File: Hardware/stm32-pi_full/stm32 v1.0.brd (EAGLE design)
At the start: 131.4 x 105.8 mm, 292 parts, among them J1 SOLDERJUMPERNO, J2 5-1814400-1, U1 ESP32-WROOM-32D, Y1 6MM_3.5MM_CRYSTAL

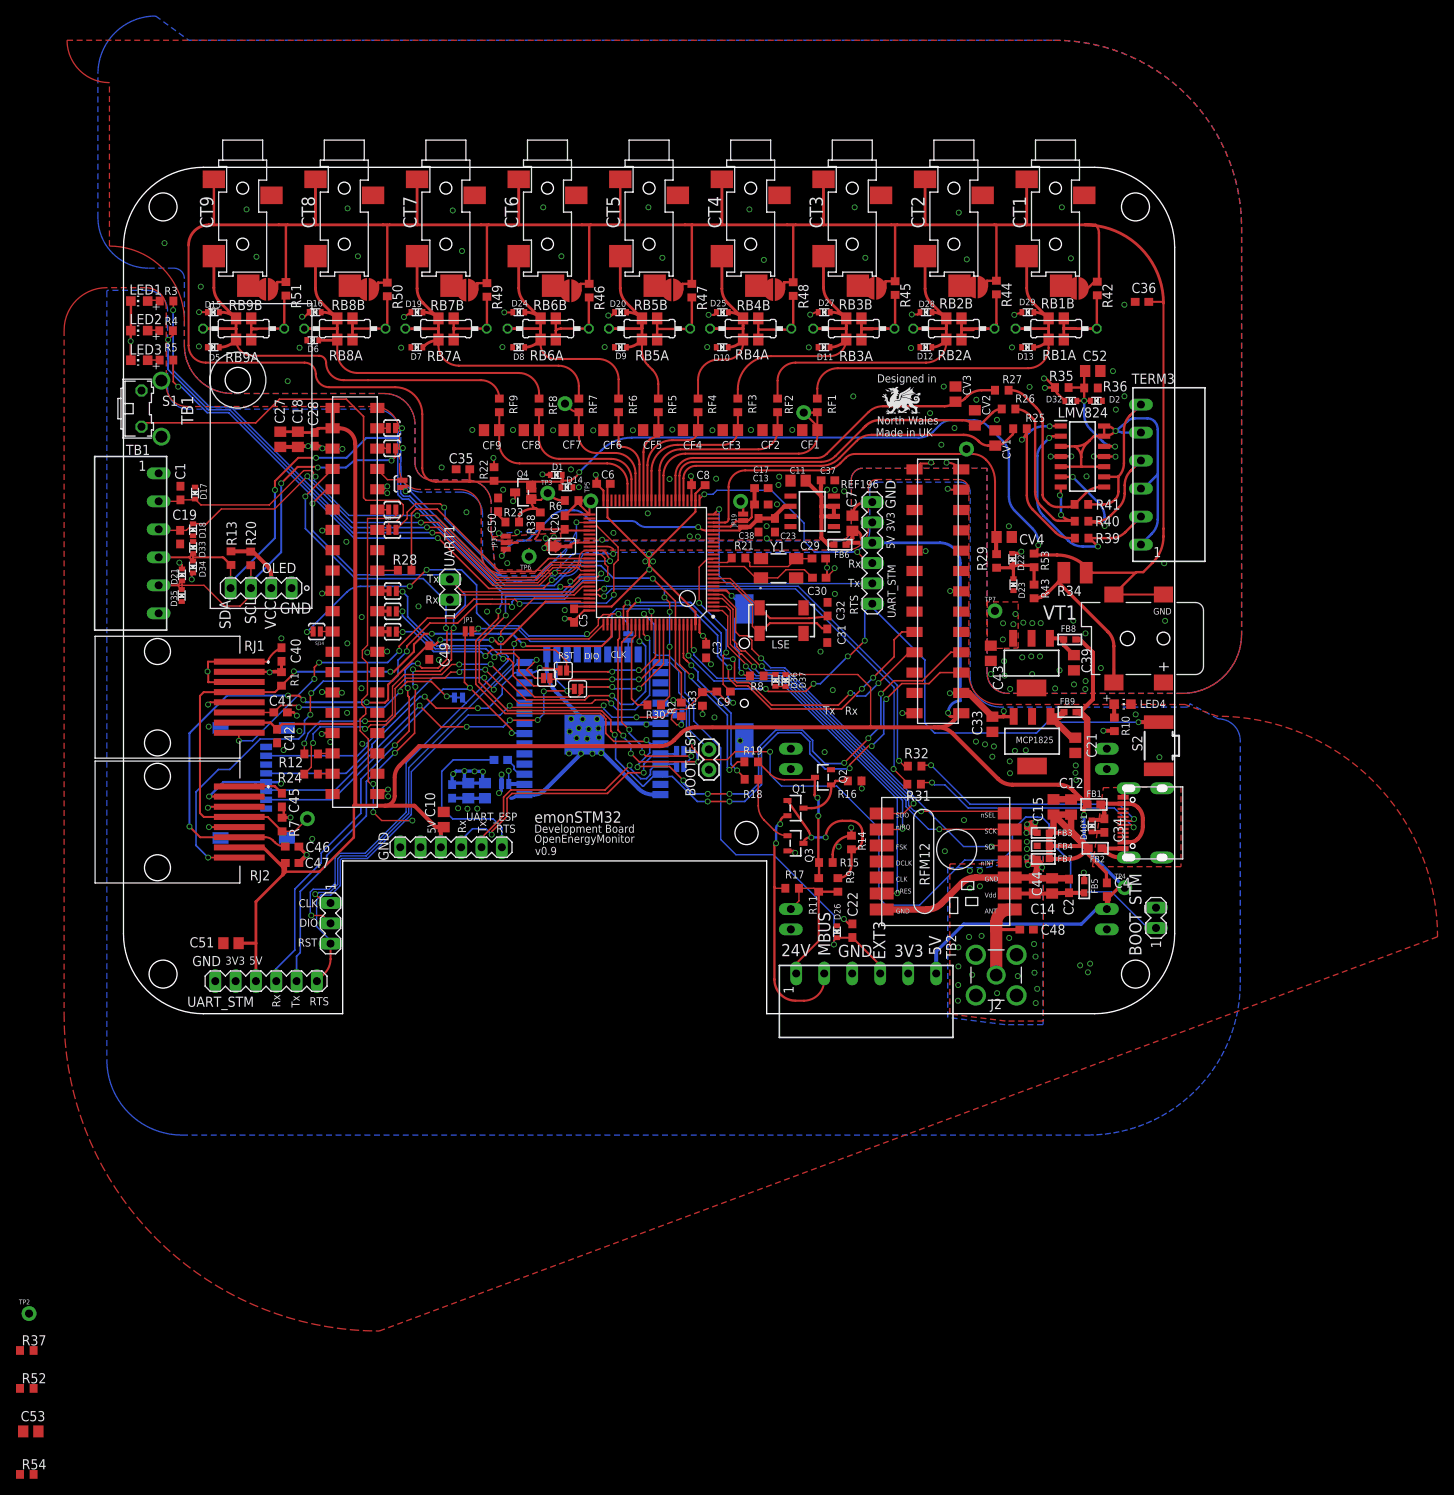
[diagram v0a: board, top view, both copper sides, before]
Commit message: UART Tx improvments and v1.0 HW change
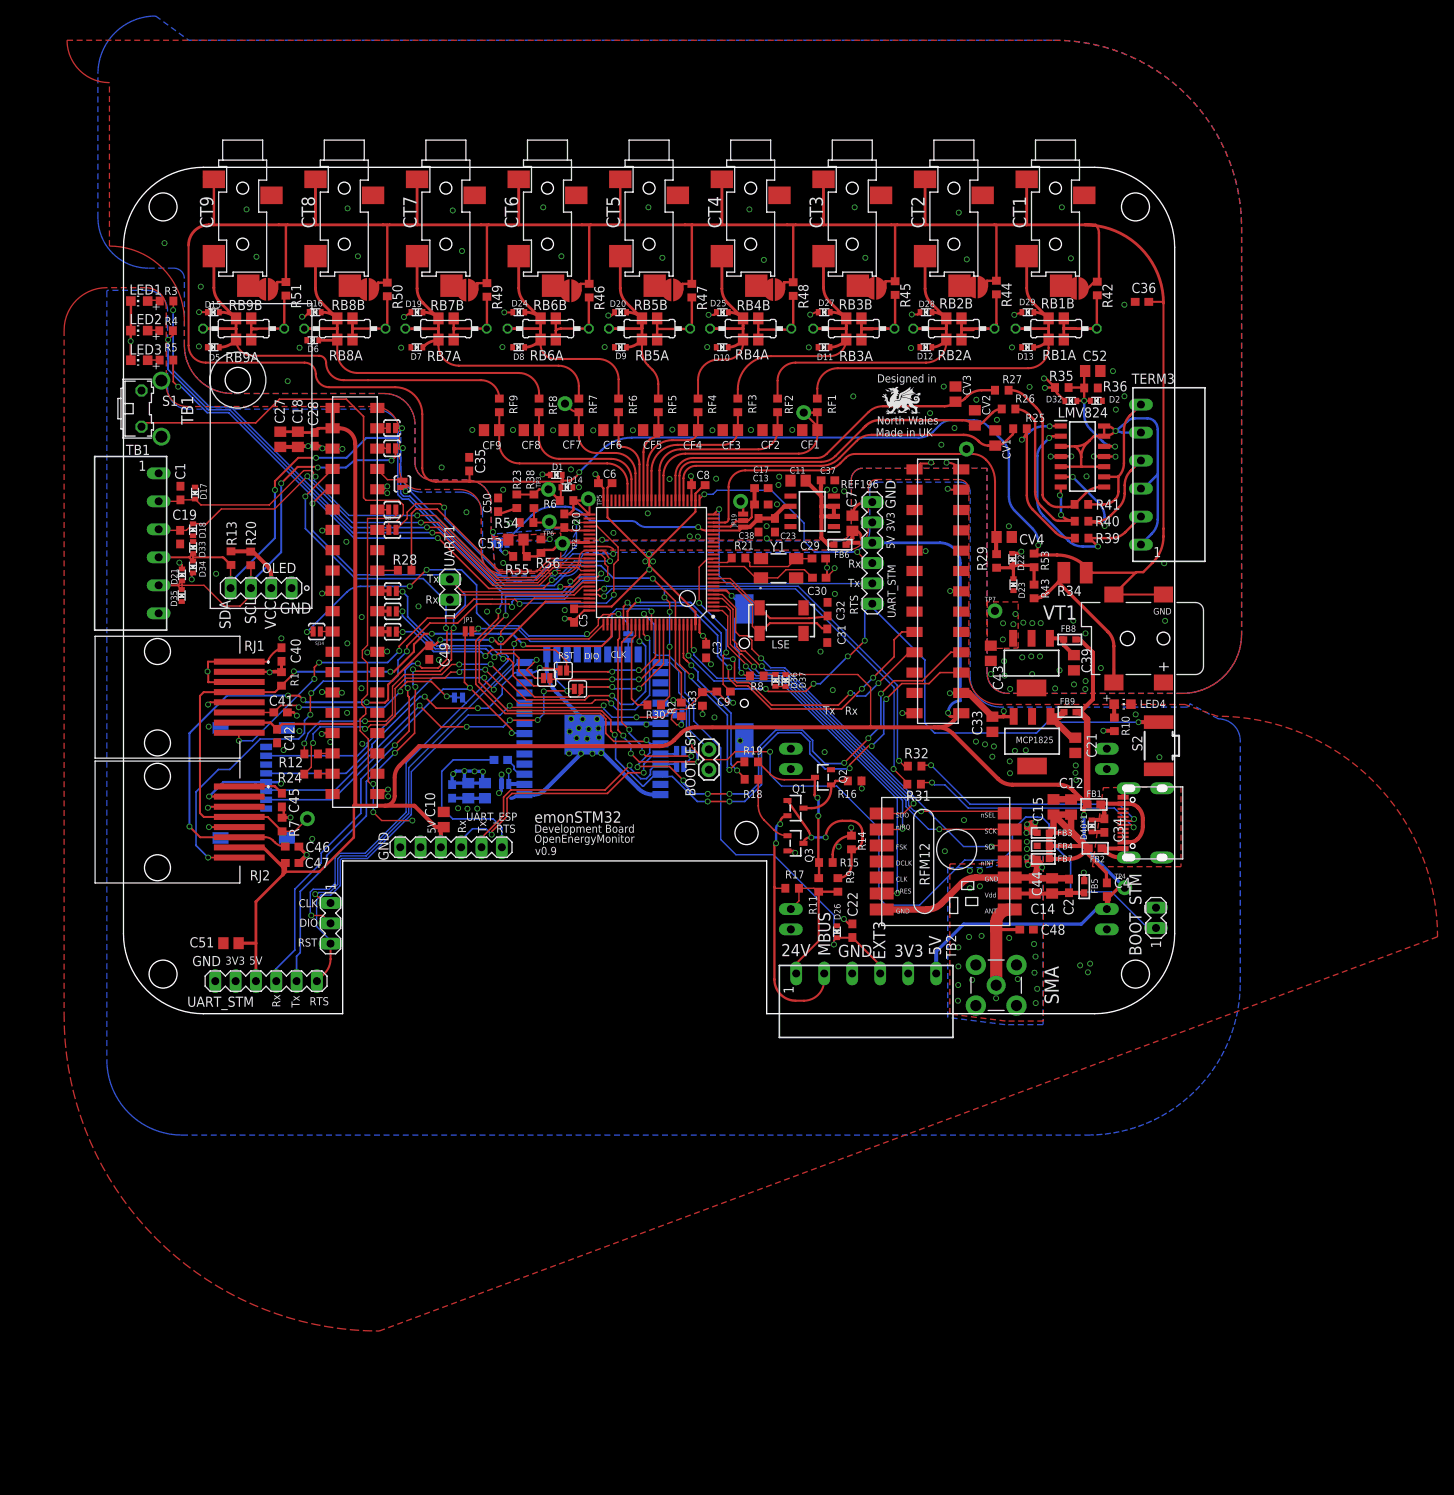
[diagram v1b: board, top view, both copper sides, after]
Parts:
- removed J2: 5-1814400-1, 5-1814400-1 sma connector:518144001
- removed JP2: JUMPER-SMT_2_NO_NO-SILK, SparkFun-Jumpers:SMT-JUMPER_2_NO_NO-SILK
- removed Q4: (no value), microbuilder:SOT23-WIDE
- removed R22, R37, R52: 10k, resistor:R0603
- removed SJ1: (no value), jumper-con_db:SJ-CON
- added R55: 9k, resistor:R0603
- added R56: 1k, resistor:R0603
- added SMA: 5-1814400-1, 5-1814400-1 sma connector:518144001
- R38: value 10k -> 4k
- R54: value 10k -> 1k
- moved R54 134.4 mm to (50.4, 61.4), turned to 180 degrees
- moved C53 126.9 mm to (49.1, 59.3), turned to 180 degrees
- moved TP2 117.1 mm to (54.9, 58.8)
- moved TP6 5.02 mm to (53.2, 61.5)
- moved R23 2.66 mm to (49.2, 64.1), turned to 90 degrees
- moved R38 2.38 mm to (51.3, 64.1)
- moved C35 1.01 mm to (43.2, 68.7), turned to 90 degrees
- moved JP3 0.66 mm to (47.1, 58.9), flipped to the bottom, turned to 0 degrees
- moved R6 0.64 mm to (55.4, 64.1)
- moved TP3 0.48 mm to (53.1, 65.5)
- moved TP5 0.40 mm to (58.1, 64.3)
- moved C6 0.24 mm to (60.2, 66.3)
- moved C20 0.23 mm to (55.1, 61.6)
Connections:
- removed net OPAMP_FB2: JP2.1, Q4.1, R23.2, R38.1, R6.2, TP3.1
- removed net OPAMP_NON-INV+: C53.1, R37.1, R52.2, TP2.1
- net +3V3ANA: no longer Q4.3
- net AGND: now also R56.1; no longer R22.1, R52.1, SJ1.2
- net ANT: now also SMA.1; no longer J2.1
- net BIAS: now also R23.2, R38.1, R6.2, TP3.1; no longer JP2.2, Q4.2, R22.2
- net N$12: now also R55.2; no longer R37.2
- net OPAMP_NON-INVERT+: now also C53.1, R55.1, R56.2, TP2.1; no longer SJ1.1
- net RGND: now also SMA.2, SMA.3, SMA.4, SMA.5; no longer J2.2, J2.3, J2.4, J2.5
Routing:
- net OPAMP_FB2: track 10.3 -> 0.00 mm
- net OPAMP_NON-INVERT+: track 2.74 -> 12.3 mm
- net BIAS: track 486.8 -> 493.3 mm
- net AGND: track 22.8 -> 18.2 mm, vias 106 -> 103
- net VREF+: track 41.2 -> 39.5 mm, vias 2 -> 1
- net N$12: track 1.50 -> 3.25 mm, vias 0 -> 1
- net ANT: track 11.8 -> 13.1 mm
- net N$7: track 1.69 -> 2.83 mm
- net OPAMP_OUT: track 11.3 -> 12.3 mm
- net +3V3ANA: track 51.0 -> 50.2 mm, vias 21 -> 20
- net BUTTON1_STM: track 35.0 -> 35.5 mm
- net DGND: track 184.9 -> 185.1 mm, vias 97 -> 98

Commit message: commit v1.0 HW for prototype.
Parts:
- removed D14, D22, D23, D32, D36, D37: ESD5Z3.3T1G, microbuilder:SOD-523
- removed EXPANSION: TSM-113-01-T-DV, pinhead+:2X13_SMT
- removed JP19, JP3: JUMPER-SMT_3_NO_NO-SILK, SparkFun-Jumpers:SMT-JUMPER_3_NO_NO-SILK
- removed R35, R36: 10k, rcl:R0603
- removed SV1: (no value), con-lstb-db:MA06-1
- removed UART1: (no value), con-lstb-db:MA02-1
- added D3: SCHOTTKY_MBR0520LT1GDO-219-AB(SOD123F), Diode:SODFL3718X115
- added D4: ESD5Z3.3T1G, microbuilder:SOD-523
- added IC2: AD8519KS, analog-devices:SC70-5
- added IC_VBAT: AP7313-33SRG-7, AP7313-33SRG-7:SOT96P240X135-3N
- added JP2: PINHD-2X7, Connector:2X07
- added R22: 0R, rcl:R0603
- added TP8: TEST-POINTPOGO_PTH, SparkFun-Connectors:1X01_NO_SILK
- C23, C50: value 1uf -> 1uF
- C49: value 1nF -> 100nF
- C52: value 22UF -> 1uF; device rcl:C0805 -> resistor:C0603
- C7: value 22uF -> 1uF; device rcl:C0805 -> resistor:C0603
- D2: value ESD5Z3.3T1G -> SCHOTTKY_MBR0520LT1GDO-219-AB(SOD123F); device microbuilder:SOD-523 -> Diode:SODFL3718X115
- J1, SJ14, SJ26, SJ27, SJ3, SJ32, SJ5, SJ6, SJ7: value SOLDERJUMPERNO -> JUMPER-SMT_2_NC_TRACE_NO-SILK; device SparkFun:SJ_2S-NO -> SparkFun-Jumpers:SMT-JUMPER_2_NC_TRACE_NO-SILK
- Q1: value (none) -> PNP
- Q2, Q3: value (none) -> NPN
- R12, R24, R28: value 10K -> 10k
- R38: value 4k -> 39k
- R39, R40, R41: value 620 -> 620R
- R54, R56: value 1k -> 10k
- R55: value 9k -> 91k
- R6: value 20R -> 0R
- R8: value 100k -> 10k
- RB1A, RB2A, RB3A, RB4A, RB5A, RB6A, RB7A, RB8A, RB9A: value 22r -> 6R8
- RB1B, RB2B, RB3B, RB4B, RB5B, RB6B, RB7B, RB8B, RB9B: value 22r -> (none)
- USART1: value (none) -> UART1
- moved D2 82.9 mm to (38.7, 77.1), turned to 180 degrees
- moved D1 58.6 mm to (111.3, 54.6), turned to 0 degrees
- moved C52 49.7 mm to (88.0, 43.3), turned to 90 degrees
- moved C7 21.1 mm to (81.9, 42.3)
- moved C11 13.8 mm to (97.5, 62.5), turned to 270 degrees
- moved FB6 12.9 mm to (101.2, 64.2)
- moved C37 8.85 mm to (95.4, 61.7), turned to 270 degrees
- moved PS1 4.49 mm to (90.6, 62.7)
- moved R41 4.14 mm to (119.8, 67.8)
- moved LMV824 4.14 mm to (119.9, 73.8)
- moved R39 4.14 mm to (119.8, 63.6)
- moved R40 4.14 mm to (119.8, 65.7)
- moved R54 2.76 mm to (47.6, 61.6)
- moved R23 2.63 mm to (46.5, 64.2)
- moved C50 2.51 mm to (44.4, 64.3)
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- renumbered D40*1 to D40, UART_STM to USART1, Y1 to HSE
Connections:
- removed net 3PH_BIAS_IN: C52.1, D2.K, D32.A, LMV824.12, R35.2, R36.1
- removed net CT_EX1: EXPANSION.3
- removed net CT_EX2: EXPANSION.6
- removed net CT_EX3: EXPANSION.5
- removed net CT_EX4: EXPANSION.8
- removed net CT_EX5: EXPANSION.7
- removed net CT_EX6: EXPANSION.10
- removed net IO1_EX: EXPANSION.15
- removed net IO2_EX: EXPANSION.16
- removed net IO4_EX: EXPANSION.18
- removed net IO6_EX: EXPANSION.21
- removed net IO7_EX: EXPANSION.23
- removed net N$12: JP3.2, R55.2
- removed net N$19: D37.K, R8.1
- removed net SINGLEPHASE_: D22.A, D23.K, R29.1, R43.1, R53.1
- removed net UART2_RX: STM32F303VE.26, SV1.4
- removed net UART2_TX: STM32F303VE.25, SV1.5
- removed net VDDA: C13.1, C17.1, JP19.2, STM32F303VE.22
- new net N$28: JP2.13
- new net _AC1: R34.1, R43.2, VT1.PWR2
- net +3V3: now also JP2.12; no longer EXPANSION.24, EXPANSION.4
- net +3V3ANA: now also C13.1, C17.1, D2.1, D4.K, IC2.5, R22.1, STM32F303VE.22; no longer D1.K, D22.K, D32.K, JP19.1, JP3.3, R35.1
- net +5V: now also C52.1, IC_VBAT.3, JP2.14; no longer C7.1, D36.A, EXPANSION.26, SV1.3
- net AC1: now also D1.K, D4.A, R29.1, R43.1, R53.1; no longer R34.1, R43.2, VT1.PWR2
- net AGND: now also D1.A, D3.2, IC2.2; no longer C11.2, C37.2, C52.2, D14.A, D2.A, D23.A, EXPANSION.1, EXPANSION.2, PS1.4, R36.2
- net BIAS: now also D2.2, D3.1, LMV824.12; no longer D1.A, D14.K
- net CAN_RX: now also JP2.7; no longer EXPANSION.17
- net CAN_TX: now also JP2.5; no longer EXPANSION.19
- net DGND: now also C11.2, C37.2, C52.2, IC_VBAT.1, JP2.2, PS1.4; no longer EXPANSION.14, EXPANSION.25, EXPANSION.9, SV1.1
- net N$16: now also C7.1, IC_VBAT.2, R8.1; no longer D36.K, D37.A
- net NRST_STM: no longer SV1.6
- net OPAMP_INVERT-: now also IC2.4
- net OPAMP_NON-INVERT+: now also IC2.3
- net OPAMP_OUT: now also IC2.1
- net SCL: now also JP2.10; no longer EXPANSION.22
- net SDA: now also JP2.8; no longer EXPANSION.20
- net UART1_RX: no longer UART1.1
- net UART1_TX: no longer UART1.2
- net VREF+: now also R22.2, R55.2, TP8.1; no longer JP19.3, JP3.1
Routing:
- net BIAS: track 493.3 -> 525.0 mm, vias 2 -> 4
- net UART2_TX: track 28.9 -> 0.00 mm, vias 1 -> 0
- net UART2_RX: track 27.3 -> 0.00 mm, vias 2 -> 0
- net _AC1: track 0.00 -> 24.7 mm
- net AC1: track 24.7 -> 7.96 mm
- net +5V: track 363.8 -> 347.3 mm, vias 2 -> 3
- net 3PH_BIAS_IN: track 16.4 -> 0.00 mm, vias 2 -> 0
- net VREF+: track 39.5 -> 50.8 mm
- net CAN_TX: track 49.6 -> 59.2 mm, vias 4 -> 2
- net SINGLEPHASE_: track 9.60 -> 0.00 mm
- net DGND: track 185.1 -> 175.8 mm, vias 98 -> 104
- net SDA: track 192.3 -> 201.6 mm
- net VDDA: track 9.02 -> 0.00 mm
- net NRST_STM: track 209.8 -> 201.5 mm, vias 13 -> 11
- net SCL: track 201.5 -> 209.6 mm
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- added copper zone on layer 1, net +3V3
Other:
- board text added: "REF19x"
- board text added: "v1.0"
- board text removed: "REF196"
- board text removed: "UART_STM"
- board text removed: "v0.9"

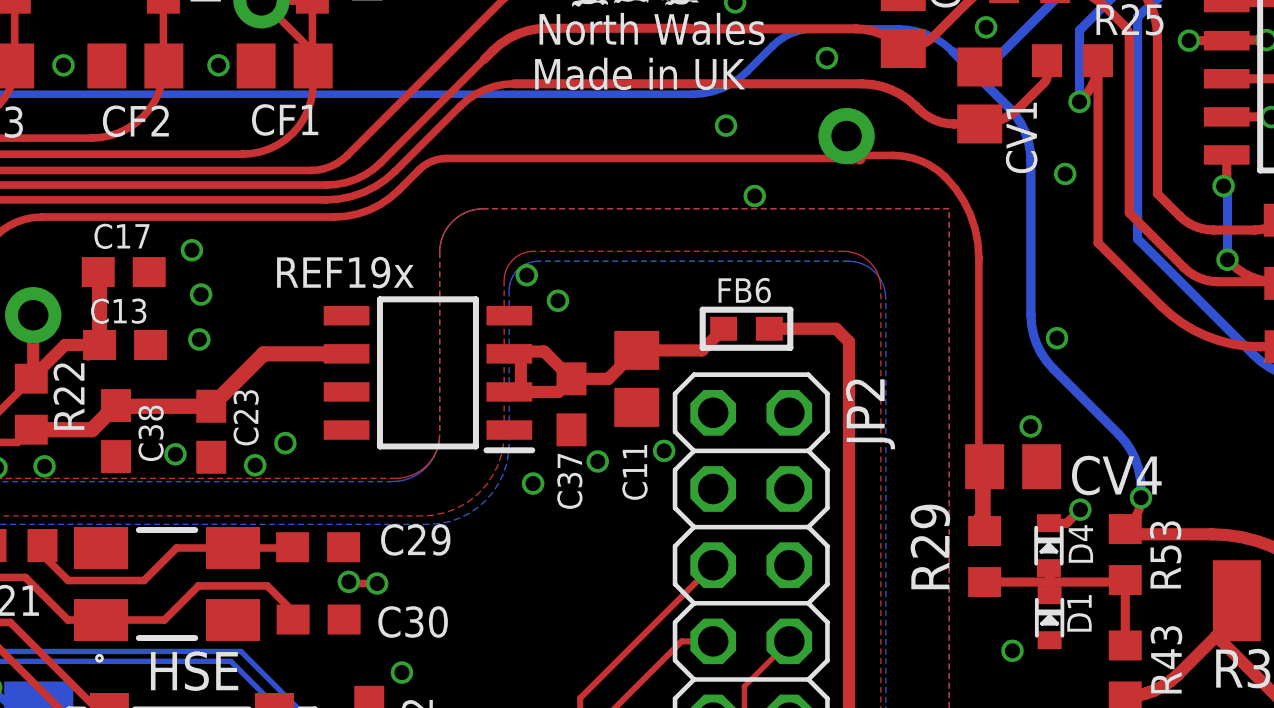
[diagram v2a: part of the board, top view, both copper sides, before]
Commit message: correct rotation of p&p'd parts.
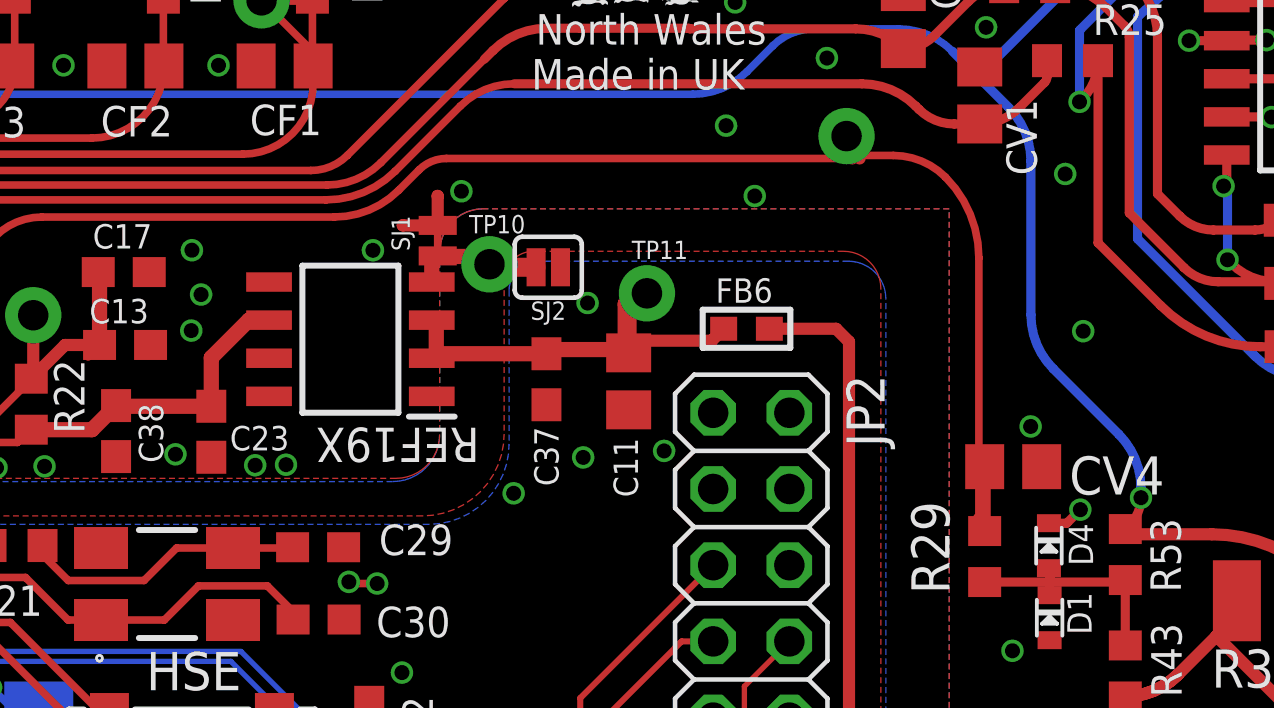
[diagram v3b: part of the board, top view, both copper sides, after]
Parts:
- removed PS1: REF191ESZ, LT1461AIS8:SOIC127P599X175-8N
- added REF19X: REF191ESZ, LT1461AIS8:SOIC127P599X175-8N
- added SJ1: JUMPER-SMT_2_NC_TRACE_NO-SILK, SparkFun-Jumpers:SMT-JUMPER_2_NC_TRACE_NO-SILK
- added SJ2: JUMPER-SMT_2_NO_SILK, SparkFun-Jumpers:SMT-JUMPER_2_NO_SILK
- added TP10, TP11: TEST-POINTPOGO_PTH, SparkFun-Connectors:1X01_NO_SILK
- moved C37 1.18 mm to (94.5, 62.5)
- moved C11 0.28 mm to (97.3, 62.4)
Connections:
- new net N$12: REF19X.4, SJ1.2, SJ2.2, TP10.1
- net +5V_REF: now also REF19X.2, REF19X.3, TP11.1; no longer PS1.2, PS1.3
- net AGND: now also SJ1.1
- net DGND: now also SJ2.1; no longer PS1.4
- net VREF+: now also REF19X.6; no longer PS1.6
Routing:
- net N$12: track 0.00 -> 4.40 mm
- net AGND: track 14.1 -> 16.3 mm, vias 115 -> 117
- net +5V_REF: track 12.2 -> 13.8 mm
- net VREF+: track 50.8 -> 49.6 mm
- net DGND: vias 104 -> 103
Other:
- board text removed: "REF19x"
